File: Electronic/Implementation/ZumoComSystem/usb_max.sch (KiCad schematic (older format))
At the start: 5 parts, among them J1 USB_A, U3 MAX3421EEHJ+T, Y1 Crystal_GND24

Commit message: Coutouts, BOM, ...
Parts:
- added R3: 0, Resistor_SMD:R_0603_1608Metric_Pad1.05x0.95mm_HandSolder, symbol Device:R
- added R4: DNP, Resistor_SMD:R_0603_1608Metric_Pad1.05x0.95mm_HandSolder, symbol Device:R
- added R5: 2.2k, Resistor_SMD:R_0603_1608Metric_Pad1.05x0.95mm_HandSolder, symbol Device:R
- C7, C8: Manufacturer (none) -> KEMET; Part-No. (none) -> C0603C180J5GAC7867
- J1: value USB_A -> USB_A_Molex_105057; Manufacturer (none) -> Molex; Part-No. (none) -> 1050570001
- U3: footprint QFP50P700X700X120-32N -> footprints:QFN50P500X500X80-33N_Generell; AVAILABILITY Unavailable -> (none); DESCRIPTION Ic Usb Periph/Host Cntrl 32tqfp - Max3421eehj+t -> (none); MF Maxim Integrated -> (none); MP MAX3421EEHJ+T -> (none); Manufacturer (none) -> Maxim Integrated; PACKAGE TQFP-32 Maxim -> (none); PRICE None -> (none); Part-No. (none) -> MAX3421EEHJ+T
- Y1: value Crystal_GND24 -> FL1200112_12MHz; Manufacturer (none) -> Diodes Incorporated; Part-No. (none) -> FL1200112
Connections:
- net +3V3: now also U3.2 (VL), R4.1, R5.1; no longer U3.12 (~RES)
- net INT: now also R5.2
- new net: R3.1, R4.2, U3.12 (~RES)
- new net ESP_EN: R3.2
- no-connect marks 19 -> 18
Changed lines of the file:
@@
 Sheet 3 7
 Title "Zumo Communication System"
-Date "2022-03-25"
+Date "2022-04-15"
 Rev "V1.0"
 Comp "NewTec GmbH"
@@
 AR Path="/60C500E6/60C6499B" Ref="J1"  Part="1"
 F 0 "J1" H 2307 4417 50  0000 C CNN
-F 1 "USB_A" H 2307 4326 50  0000 C CNN
+F 1 "USB_A_Molex_105057" H 2307 4326 50  0000 C CNN
 F 2 "footprints:USB_A_Molex_105057_Vertical_2" H 2400 3900 50  0001 C CNN
-F 3 " ~" H 2400 3900 50  0001 C CNN
+F 3 "https://www.molex.com/pdm_docs/ps/PS-105057-001.pdf" H 2400 3900 50  0001 C CNN
+F 4 "Molex" H 2250 3950 50  0001 C CNN "Manufacturer"
+F 5 "1050570001" H 2250 3950 50  0001 C CNN "Part-No."
 	1    2250 3950
 	1    0    0    -1
@@
 F 0 "U3" H 5350 4420 50  0000 C CNN
 F 1 "MAX3421EEHJ+T" H 5350 4329 50  0000 C CNN
-F 2 "QFP50P700X700X120-32N" H 5350 2950 50  0001 L BNN
+F 2 "footprints:QFN50P500X500X80-33N_Generell" H 5350 2950 50  0001 L BNN
 F 3 "https://eu.mouser.com/datasheet/2/256/MAX3421E-1513231.pdf" H 5350 2950 50  0001 L BNN
-F 4 "Maxim Integrated" H 5350 2950 50  0001 L BNN "MF"
-F 5 "Ic Usb Periph/Host Cntrl 32tqfp - Max3421eehj+t" H 5350 2950 50  0001 L BNN "DESCRIPTION"
-F 6 "MAX3421EEHJ+T" H 5350 2950 50  0001 L BNN "MP"
-F 7 "TQFP-32 Maxim" H 5350 2950 50  0001 L BNN "PACKAGE"
-F 8 "None" H 5350 2950 50  0001 L BNN "PRICE"
-F 9 "Unavailable" H 5350 2950 50  0001 L BNN "AVAILABILITY"
+F 4 "Maxim Integrated" H 5350 2950 50  0001 C CNN "Manufacturer"
+F 5 "MAX3421EEHJ+T" H 5350 2950 50  0001 C CNN "Part-No."
 	1    5350 2950
 	1    0    0    -1
@@
 	4650 2050 4250 2050
 Wire Wire Line
-	6050 2050 6450 2050
+	6050 2050 6250 2050
 Wire Wire Line
 	4650 3650 4250 3650
@@
 	6150 4250 6150 4350
 Wire Wire Line
-	6050 1750 6450 1750
-Wire Wire Line
-	6450 1750 6450 1650
-Wire Wire Line
-	4650 1950 4250 1950
+	6050 1750 6250 1750
+Wire Wire Line
+	6250 1750 6250 1650
 $Comp
 L power:GND #PWR021
@@
 	2200 4450 2250 4450
 Wire Wire Line
-	2550 3750 2650 3750
-Wire Wire Line
-	2650 3750 2650 3650
+	2550 3750 2900 3750
+Wire Wire Line
+	2900 3750 2900 3650
 $Comp
 L power:+5V #PWR017
 U 1 1 61716434
-P 2650 3650
-F 0 "#PWR017" H 2650 3500 50  0001 C CNN
-F 1 "+5V" H 2665 3823 50  0000 C CNN
-F 2 "" H 2650 3650 50  0001 C CNN
-F 3 "" H 2650 3650 50  0001 C CNN
-	1    2650 3650
+P 2900 3650
+F 0 "#PWR017" H 2900 3500 50  0001 C CNN
+F 1 "+5V" H 2915 3823 50  0000 C CNN
+F 2 "" H 2900 3650 50  0001 C CNN
+F 3 "" H 2900 3650 50  0001 C CNN
+	1    2900 3650
 	1    0    0    -1
 $EndComp
@@
 L power:+3.3V #PWR022
 U 1 1 61716978
-P 6450 1650
-F 0 "#PWR022" H 6450 1500 50  0001 C CNN
-F 1 "+3.3V" H 6465 1823 50  0000 C CNN
-F 2 "" H 6450 1650 50  0001 C CNN
-F 3 "" H 6450 1650 50  0001 C CNN
-	1    6450 1650
+P 6250 1650
+F 0 "#PWR022" H 6250 1500 50  0001 C CNN
+F 1 "+3.3V" H 6265 1823 50  0000 C CNN
+F 2 "" H 6250 1650 50  0001 C CNN
+F 3 "" H 6250 1650 50  0001 C CNN
+	1    6250 1650
 	1    0    0    -1
 $EndComp
@@
 L power:+3.3V #PWR020
 U 1 1 61716F75
-P 4250 1650
-F 0 "#PWR020" H 4250 1500 50  0001 C CNN
-F 1 "+3.3V" H 4265 1823 50  0000 C CNN
-F 2 "" H 4250 1650 50  0001 C CNN
-F 3 "" H 4250 1650 50  0001 C CNN
-	1    4250 1650
-	1    0    0    -1
-$EndComp
-Wire Wire Line
-	4250 1650 4250 1950
-NoConn ~ 4650 2150
+P 4400 1650
+F 0 "#PWR020" H 4400 1500 50  0001 C CNN
+F 1 "+3.3V" H 4415 1823 50  0000 C CNN
+F 2 "" H 4400 1650 50  0001 C CNN
+F 3 "" H 4400 1650 50  0001 C CNN
+	1    4400 1650
+	1    0    0    -1
+$EndComp
 NoConn ~ 4650 2250
 NoConn ~ 4650 2450
@@
 F 2 "Capacitor_SMD:C_0603_1608Metric_Pad1.05x0.95mm_HandSolder" H 1588 6200 50  0001 C CNN
 F 3 "~" H 1550 6350 50  0001 C CNN
+F 4 "KEMET" H 1550 6350 50  0001 C CNN "Manufacturer"
+F 5 "C0603C180J5GAC7867" H 1550 6350 50  0001 C CNN "Part-No."
 	1    1550 6350
 	1    0    0    -1
@@
 F 2 "Capacitor_SMD:C_0603_1608Metric_Pad1.05x0.95mm_HandSolder" H 3038 6200 50  0001 C CNN
 F 3 "~" H 3000 6350 50  0001 C CNN
+F 4 "KEMET" H 3000 6350 50  0001 C CNN "Manufacturer"
+F 5 "C0603C180J5GAC7867" H 3000 6350 50  0001 C CNN "Part-No."
 	1    3000 6350
 	1    0    0    -1
@@
 Wire Wire Line
 	4050 3450 4650 3450
-$Comp
-L Device:Crystal_GND24 Y1
-U 1 1 623EF4A9
-P 2250 5950
-F 0 "Y1" H 2444 5996 50  0000 L CNN
-F 1 "Crystal_GND24" H 2000 5100 50  0000 L CNN
-F 2 "Crystal:Crystal_SMD_3225-4Pin_3.2x2.5mm_HandSoldering" H 2250 5950 50  0001 C CNN
-F 3 "https://www.diodes.com/assets/Datasheets/FL.pdf" H 2250 5950 50  0001 C CNN
-	1    2250 5950
-	1    0    0    -1
-$EndComp
 Wire Wire Line
 	1550 5300 1550 5950
@@
 Wire Wire Line
 	1550 5950 1550 6200
+$Comp
+L Device:Crystal_GND24 Y1
+U 1 1 623EF4A9
+P 2250 5950
+F 0 "Y1" H 2444 5996 50  0000 L CNN
+F 1 "FL1200112_12MHz" H 1900 6700 50  0000 L CNN
+F 2 "Crystal:Crystal_SMD_3225-4Pin_3.2x2.5mm_HandSoldering" H 2250 5950 50  0001 C CNN
+F 3 "https://www.diodes.com/assets/Datasheets/FL.pdf" H 2250 5950 50  0001 C CNN
+F 4 "Diodes Incorporated" H 2250 5950 50  0001 C CNN "Manufacturer"
+F 5 "FL1200112" H 2250 5950 50  0001 C CNN "Part-No."
+	1    2250 5950
+	1    0    0    -1
+$EndComp
+Wire Wire Line
+	4650 2150 4400 2150
+$Comp
+L Device:R R5
+U 1 1 6256E0B6
+P 6250 1900
+F 0 "R5" H 6320 1946 50  0000 L CNN
+F 1 "2.2k" H 6320 1855 50  0000 L CNN
+F 2 "Resistor_SMD:R_0603_1608Metric_Pad1.05x0.95mm_HandSolder" V 6180 1900 50  0001 C CNN
+F 3 "~" H 6250 1900 50  0001 C CNN
+F 4 "TE Connectivity Passive Product" H 6250 1900 50  0001 C CNN "Manufacturer"
+F 5 "CRGCQ0603J2K2" H 6250 1900 50  0001 C CNN "Part-No."
+	1    6250 1900
+	1    0    0    -1
+$EndComp
+Connection ~ 6250 1750
+Connection ~ 6250 2050
+Wire Wire Line
+	6250 2050 6450 2050
+Text HLabel 3550 1950 0    50   BiDi ~ 0
+ESP_EN
+Wire Wire Line
+	4650 1950 4100 1950
+$Comp
+L Device:R R4
+U 1 1 6256E70A
+P 4100 1800
+F 0 "R4" H 4170 1846 50  0000 L CNN
+F 1 "DNP" H 4170 1755 50  0000 L CNN
+F 2 "Resistor_SMD:R_0603_1608Metric_Pad1.05x0.95mm_HandSolder" V 4030 1800 50  0001 C CNN
+F 3 "~" H 4100 1800 50  0001 C CNN
+F 4 "-" H 4100 1800 50  0001 C CNN "Manufacturer"
+F 5 "-" H 4100 1800 50  0001 C CNN "Part-No."
+	1    4100 1800
+	1    0    0    -1
+$EndComp
+Connection ~ 4100 1950
+Wire Wire Line
+	4100 1650 4400 1650
+Wire Wire Line
+	3550 1950 3700 1950
+Wire Wire Line
+	4400 2150 4400 1650
+Connection ~ 4400 1650
+$Comp
+L Device:R R3
+U 1 1 62574913
+P 3850 1950
+F 0 "R3" V 3643 1950 50  0000 C CNN
+F 1 "0" V 3734 1950 50  0000 C CNN
+F 2 "Resistor_SMD:R_0603_1608Metric_Pad1.05x0.95mm_HandSolder" V 3780 1950 50  0001 C CNN
+F 3 "~" H 3850 1950 50  0001 C CNN
+F 4 "YAGEO" H 3850 1950 50  0001 C CNN "Manufacturer"
+F 5 "RC0603FR-070RL" H 3850 1950 50  0001 C CNN "Part-No."
+	1    3850 1950
+	0    1    1    0
+$EndComp
+Wire Wire Line
+	4000 1950 4100 1950
 $EndSCHEMATC

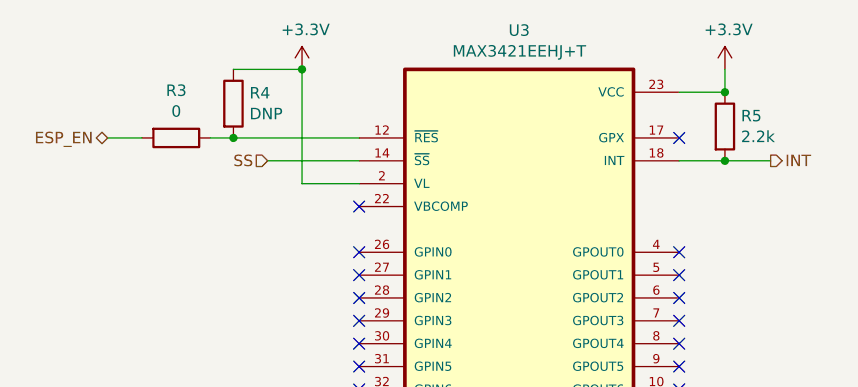
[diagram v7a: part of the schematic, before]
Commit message: replaced 3V3 Regulator
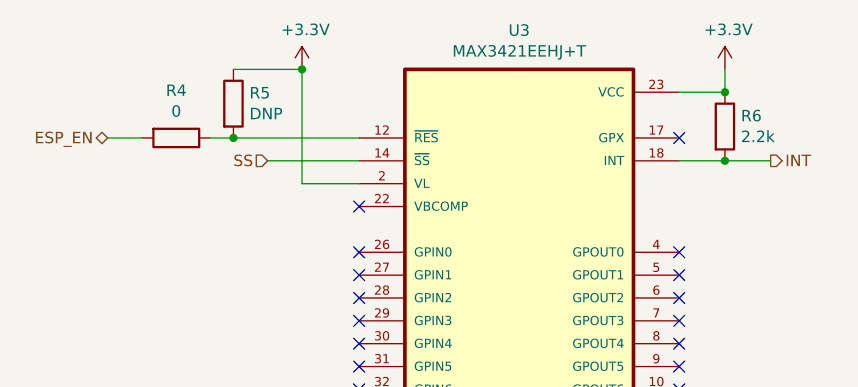
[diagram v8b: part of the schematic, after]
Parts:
- renumbered R3 to R4, R4 to R5, R5 to R6
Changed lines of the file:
@@
 Sheet 3 7
 Title "Zumo Communication System"
-Date "2022-04-15"
+Date "2022-04-22"
 Rev "V1.0"
 Comp "NewTec GmbH"
@@
 	6250 1750 6250 1650
 $Comp
-L power:GND #PWR021
+L power:GND #PWR022
 U 1 1 6171550F
 P 6150 4350
-F 0 "#PWR021" H 6150 4100 50  0001 C CNN
+F 0 "#PWR022" H 6150 4100 50  0001 C CNN
 F 1 "GND" H 6155 4177 50  0000 C CNN
 F 2 "" H 6150 4350 50  0001 C CNN
@@
 $EndComp
 $Comp
-L power:GND #PWR015
+L power:GND #PWR016
 U 1 1 617158D8
 P 2200 4450
-F 0 "#PWR015" H 2200 4200 50  0001 C CNN
+F 0 "#PWR016" H 2200 4200 50  0001 C CNN
 F 1 "GND" H 2205 4277 50  0000 C CNN
 F 2 "" H 2200 4450 50  0001 C CNN
@@
 	2900 3750 2900 3650
 $Comp
-L power:+5V #PWR017
+L power:+5V #PWR019
 U 1 1 61716434
 P 2900 3650
-F 0 "#PWR017" H 2900 3500 50  0001 C CNN
+F 0 "#PWR019" H 2900 3500 50  0001 C CNN
 F 1 "+5V" H 2915 3823 50  0000 C CNN
 F 2 "" H 2900 3650 50  0001 C CNN
@@
 $EndComp
 $Comp
-L power:+3.3V #PWR022
+L power:+3.3V #PWR023
 U 1 1 61716978
 P 6250 1650
-F 0 "#PWR022" H 6250 1500 50  0001 C CNN
+F 0 "#PWR023" H 6250 1500 50  0001 C CNN
 F 1 "+3.3V" H 6265 1823 50  0000 C CNN
 F 2 "" H 6250 1650 50  0001 C CNN
@@
 $EndComp
 $Comp
-L power:+3.3V #PWR020
+L power:+3.3V #PWR021
 U 1 1 61716F75
 P 4400 1650
-F 0 "#PWR020" H 4400 1500 50  0001 C CNN
+F 0 "#PWR021" H 4400 1500 50  0001 C CNN
 F 1 "+3.3V" H 4415 1823 50  0000 C CNN
 F 2 "" H 4400 1650 50  0001 C CNN
@@
 $EndComp
 $Comp
-L power:GND #PWR014
+L power:GND #PWR015
 U 1 1 623D7F8C
 P 1550 6500
-F 0 "#PWR014" H 1550 6250 50  0001 C CNN
+F 0 "#PWR015" H 1550 6250 50  0001 C CNN
 F 1 "GND" H 1555 6327 50  0000 C CNN
 F 2 "" H 1550 6500 50  0001 C CNN
@@
 $EndComp
 $Comp
-L power:GND #PWR019
+L power:GND #PWR020
 U 1 1 623D8337
 P 3000 6500
-F 0 "#PWR019" H 3000 6250 50  0001 C CNN
+F 0 "#PWR020" H 3000 6250 50  0001 C CNN
 F 1 "GND" H 3005 6327 50  0000 C CNN
 F 2 "" H 3000 6500 50  0001 C CNN
@@
 $EndComp
 $Comp
-L power:GND #PWR016
+L power:GND #PWR017
 U 1 1 623F4CEC
 P 2250 6500
-F 0 "#PWR016" H 2250 6250 50  0001 C CNN
+F 0 "#PWR017" H 2250 6250 50  0001 C CNN
 F 1 "GND" H 2255 6327 50  0000 C CNN
 F 2 "" H 2250 6500 50  0001 C CNN
@@
 	4650 2150 4400 2150
 $Comp
-L Device:R R5
+L Device:R R6
 U 1 1 6256E0B6
 P 6250 1900
-F 0 "R5" H 6320 1946 50  0000 L CNN
+F 0 "R6" H 6320 1946 50  0000 L CNN
 F 1 "2.2k" H 6320 1855 50  0000 L CNN
 F 2 "Resistor_SMD:R_0603_1608Metric_Pad1.05x0.95mm_HandSolder" V 6180 1900 50  0001 C CNN
@@
 	4650 1950 4100 1950
 $Comp
-L Device:R R4
+L Device:R R5
 U 1 1 6256E70A
 P 4100 1800
-F 0 "R4" H 4170 1846 50  0000 L CNN
+F 0 "R5" H 4170 1846 50  0000 L CNN
 F 1 "DNP" H 4170 1755 50  0000 L CNN
 F 2 "Resistor_SMD:R_0603_1608Metric_Pad1.05x0.95mm_HandSolder" V 4030 1800 50  0001 C CNN
@@
 Connection ~ 4400 1650
 $Comp
-L Device:R R3
+L Device:R R4
 U 1 1 62574913
 P 3850 1950
-F 0 "R3" V 3643 1950 50  0000 C CNN
+F 0 "R4" V 3643 1950 50  0000 C CNN
 F 1 "0" V 3734 1950 50  0000 C CNN
 F 2 "Resistor_SMD:R_0603_1608Metric_Pad1.05x0.95mm_HandSolder" V 3780 1950 50  0001 C CNN
